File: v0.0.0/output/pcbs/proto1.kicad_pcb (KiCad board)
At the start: 2 copper layers, 158.4 x 138 mm, 60 parts

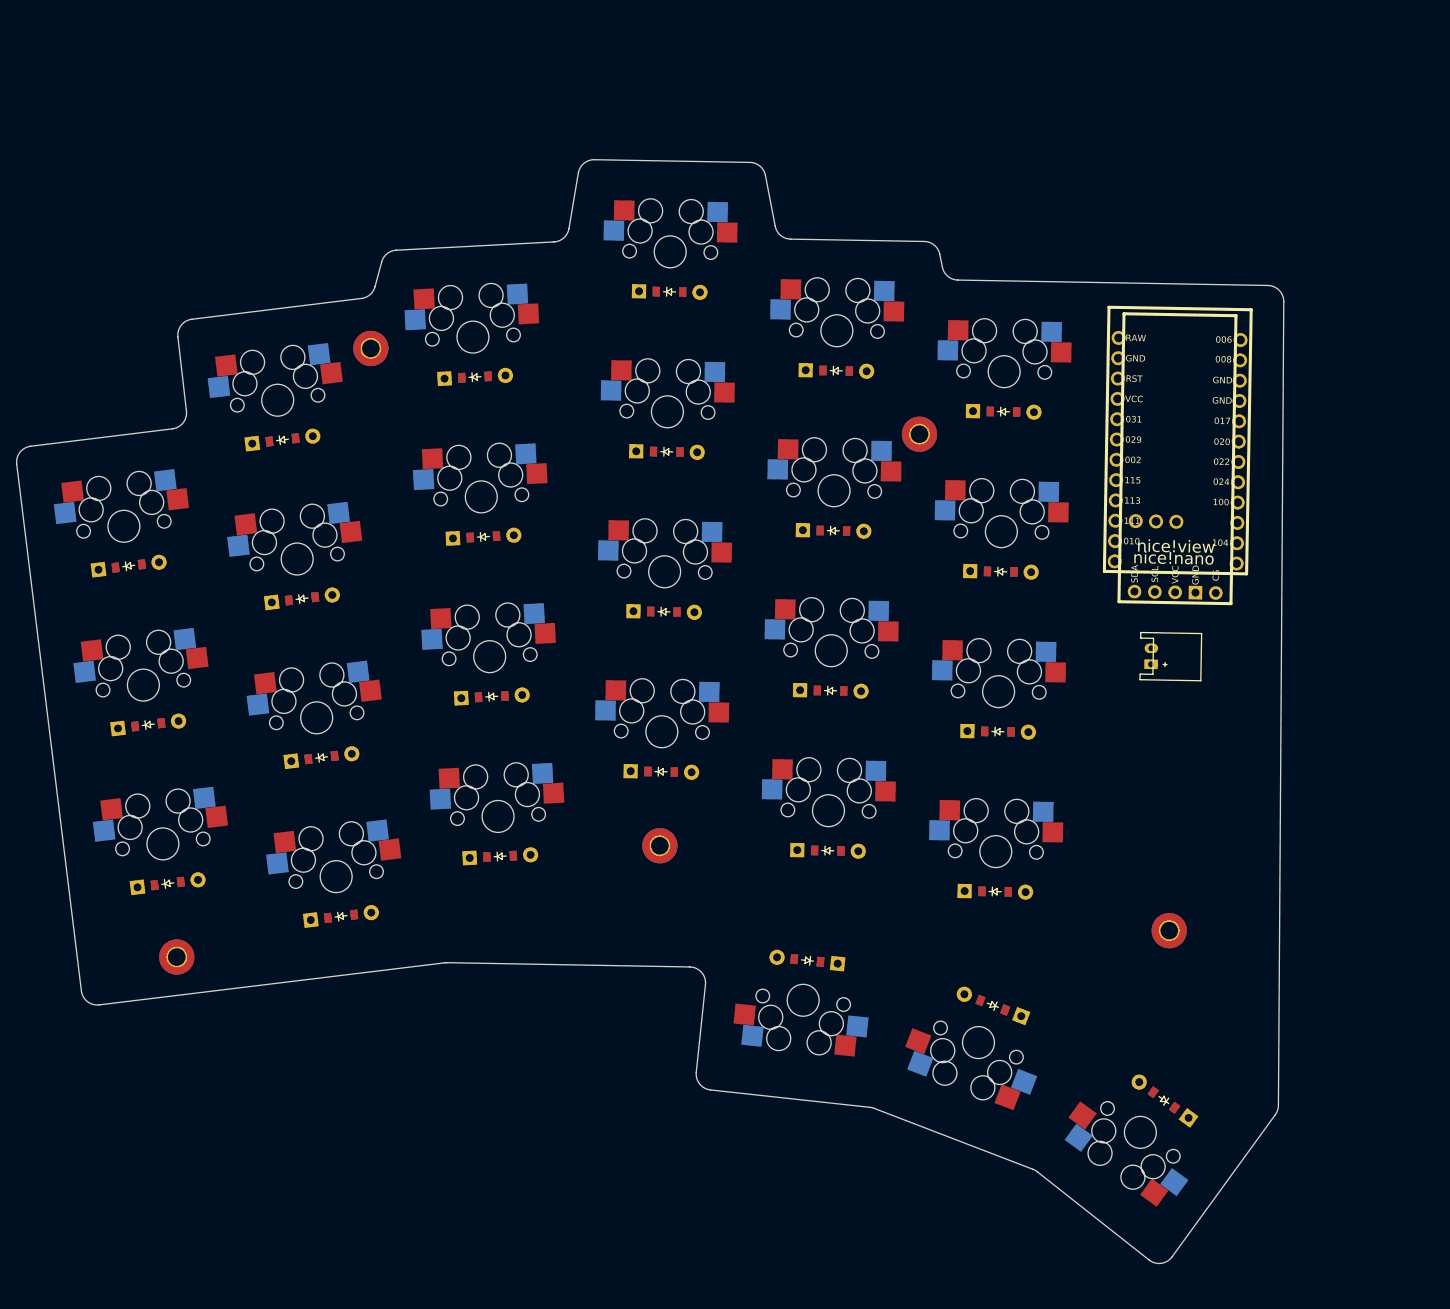
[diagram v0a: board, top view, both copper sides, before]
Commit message: footprint generator library
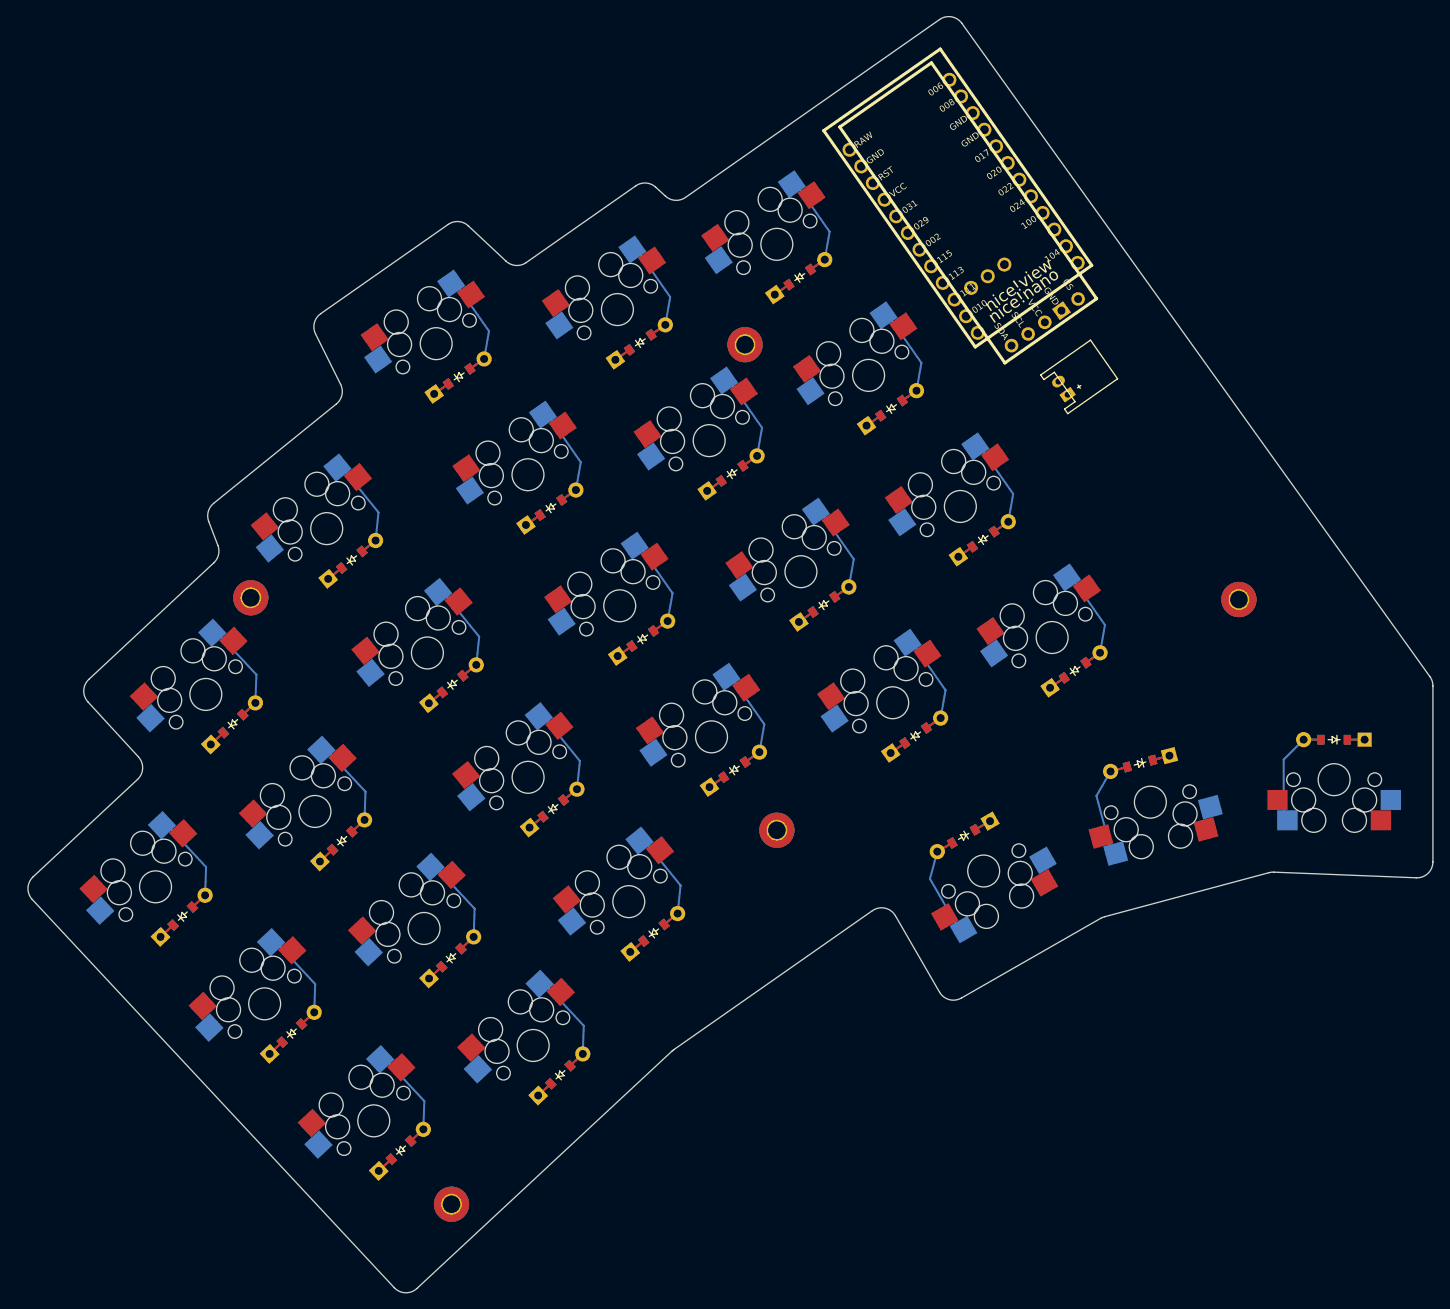
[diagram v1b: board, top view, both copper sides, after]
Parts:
- moved S26 50.3 mm to (289.4, 130.6), turned to 180 degrees
- moved D26 49.8 mm to (289.4, 125.6), turned to 180 degrees
- moved _1 46.2 mm to (179.0, 183.7), turned to 43 degrees
- moved S3 45.2 mm to (142.0, 144.0), turned to 43 degrees
- moved D3 44.3 mm to (145.4, 147.6), turned to 43 degrees
- moved D1 44.3 mm to (172.7, 176.9), turned to 43 degrees
- moved S1 43.5 mm to (169.3, 173.2), turned to 43 degrees
- moved S2 42.6 mm to (155.7, 158.6), turned to 43 degrees
- moved D2 42.5 mm to (159.1, 162.3), turned to 43 degrees
- moved _3 42.3 mm to (277.5, 108.1), turned to 35 degrees
- moved MCU1 40.6 mm to (243.0, 58.9), turned to -55 degrees
- moved S7 37.9 mm to (148.3, 119.9), turned to 43 degrees
- moved niceView1 37.4 mm to (253.9, 74.5), turned to 125 degrees
- moved S25 36.9 mm to (266.4, 133.4), turned to -165 degrees
- moved D7 36.0 mm to (151.7, 123.6), turned to 43 degrees
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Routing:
- net P002: track 0.00 -> 25.9 mm
- net P029: track 0.00 -> 25.9 mm
- net P031: track 0.00 -> 25.9 mm
- net P115: track 0.00 -> 21.6 mm
- net outer_top: track 0.00 -> 15.8 mm
- net index_num: track 0.00 -> 15.6 mm
- net pinky_num: track 0.00 -> 15.6 mm
- net inner_home: track 0.00 -> 15.6 mm
- net outer_home: track 0.00 -> 15.6 mm
- net index_top: track 0.00 -> 15.6 mm
- net middle_home: track 0.00 -> 15.6 mm
- net pinky_top: track 0.00 -> 15.6 mm
- net middle_num: track 0.00 -> 15.6 mm
- net outer_num: track 0.00 -> 15.6 mm
- net index_bottom: track 0.00 -> 15.6 mm
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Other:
- board size 158.4 x 138 mm -> 175.6 x 159.5 mm
